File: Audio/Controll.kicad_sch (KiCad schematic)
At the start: 26 parts, among them J12 Conn_01x02_Pin, J13 Conn_01x02_Pin, J14 Conn_01x02_Pin, J15 Conn_01x02_Pin, J17 Conn_01x02_Pin, K1 AZ850P2-x, K10 AZ850P2-x, K2 AZ850P2-x, K3 AZ850P2-x, K4 AZ850P2-x, K5 AZ850P2-x, K6 AZ850P2-x, K7 AZ850P2-x, K8 AZ850P2-x, K9 AZ850P2-x, U4 BP5293-50, U5 ULN2803A, U6 ULN2803A, U7 ULN2803A

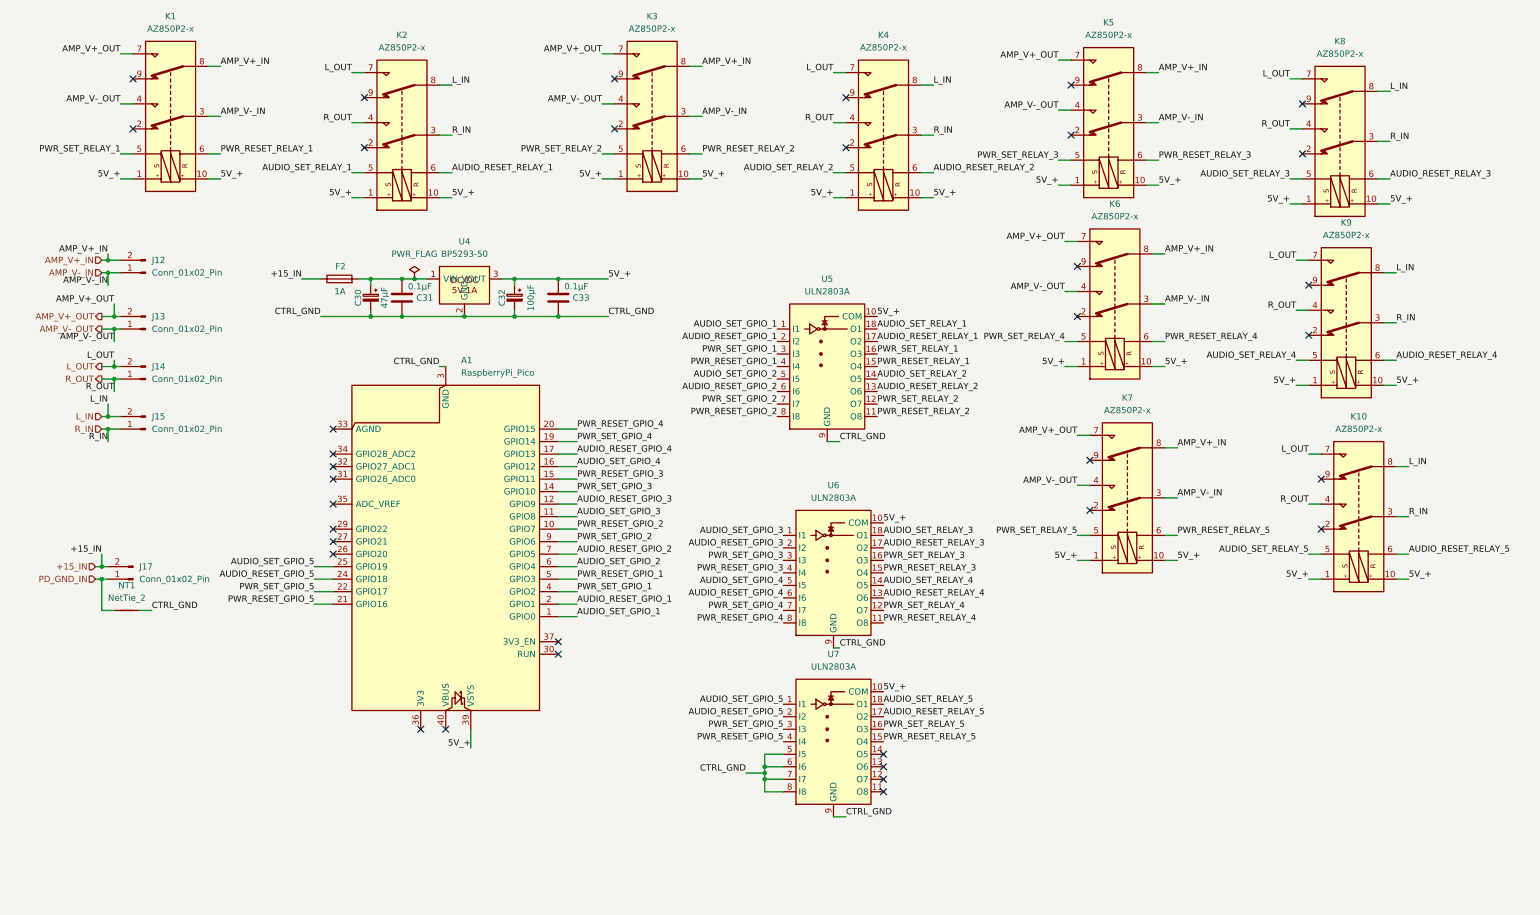
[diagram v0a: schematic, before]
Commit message: Audio: Controll端子・リレー配線とPCB部品配置まで反映。
ControllにAmp向け2P端子10個とリレー周りの回路を更新し、AudioCaseへフットプリントを配置。EQ/Amp/Controllは回路図レイアウトに合わせて部品位置を調整（PowerModuleは配線済みのため未変更）。BP5293-50フットプリント修正と配置用スクリプトを追加。

Co-authored-by: Cursor <cursoragent@cursor.com>
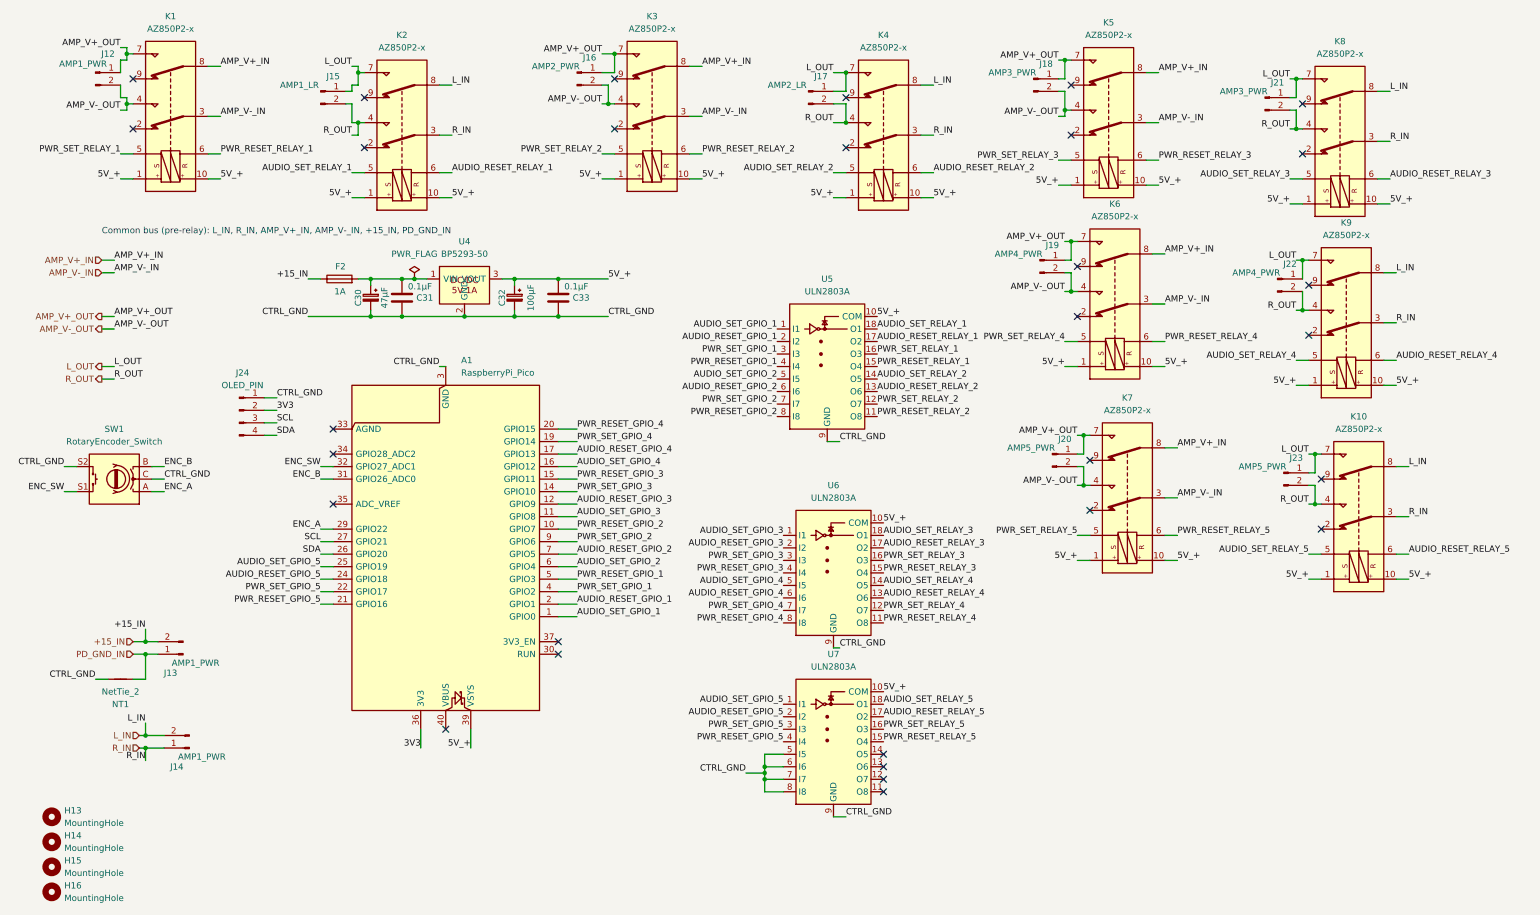
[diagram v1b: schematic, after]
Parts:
- added H13, H14, H15, H16: MountingHole, MountingHole:MountingHole_3.2mm_M3, symbol Mechanical:MountingHole
- added J16: AMP2_PWR, TerminalBlock_Phoenix:TerminalBlock_Phoenix_MKDS-1,5-2-5.08_1x02_P5.08mm_Horizontal, symbol Connector:Conn_01x02_Pin
- added J18, J21: AMP3_PWR, TerminalBlock_Phoenix:TerminalBlock_Phoenix_MKDS-1,5-2-5.08_1x02_P5.08mm_Horizontal, symbol Connector:Conn_01x02_Pin
- added J19, J22: AMP4_PWR, TerminalBlock_Phoenix:TerminalBlock_Phoenix_MKDS-1,5-2-5.08_1x02_P5.08mm_Horizontal, symbol Connector:Conn_01x02_Pin
- added J20, J23: AMP5_PWR, TerminalBlock_Phoenix:TerminalBlock_Phoenix_MKDS-1,5-2-5.08_1x02_P5.08mm_Horizontal, symbol Connector:Conn_01x02_Pin
- added J24: OLED_PIN, TerminalBlock_Phoenix:TerminalBlock_Phoenix_MKDS-1,5-4-5.08_1x04_P5.08mm_Horizontal, symbol Connector:Conn_01x04_Pin
- added SW1: RotaryEncoder_Switch, Rotary_Encoder:RotaryEncoder_Alps_EC11E-Switch_Vertical_H20mm, symbol Device:RotaryEncoder_Switch
- J12, J13, J14: value Conn_01x02_Pin -> AMP1_PWR; footprint (none) -> TerminalBlock_Phoenix:TerminalBlock_Phoenix_MKDS-1,5-2-5.08_1x02_P5.08mm_Horizontal
- J15: value Conn_01x02_Pin -> AMP1_LR; footprint (none) -> TerminalBlock_Phoenix:TerminalBlock_Phoenix_MKDS-1,5-2-5.08_1x02_P5.08mm_Horizontal
- J17: value Conn_01x02_Pin -> AMP2_LR; footprint (none) -> TerminalBlock_Phoenix:TerminalBlock_Phoenix_MKDS-1,5-2-5.08_1x02_P5.08mm_Horizontal
- NT1: footprint (none) -> NetTie:NetTie-2_THT_Pad1.0mm
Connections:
- net +15_IN: now also J13.2 (Pin_2); no longer J17.2 (Pin_2)
- net AMP_V+_IN: no longer J12.2 (Pin_2)
- net AMP_V+_OUT: now also J12.1 (Pin_1), J16.1 (Pin_1), J18.1 (Pin_1), J19.1 (Pin_1), J20.1 (Pin_1); no longer J13.2 (Pin_2)
- net AMP_V-_IN: no longer J12.1 (Pin_1)
- net AMP_V-_OUT: now also J12.2 (Pin_2), J16.2 (Pin_2), J18.2 (Pin_2), J19.2 (Pin_2), J20.2 (Pin_2); no longer J13.1 (Pin_1)
- net CTRL_GND: now also J24.1 (Pin_1), SW1.C, SW1.S2
- net L_IN: now also J14.2 (Pin_2); no longer J15.2 (Pin_2)
- net L_OUT: now also J15.1 (Pin_1), J17.1 (Pin_1), J21.1 (Pin_1), J22.1 (Pin_1), J23.1 (Pin_1); no longer J14.2 (Pin_2)
- net PD_GND_IN: now also J13.1 (Pin_1); no longer J17.1 (Pin_1)
- net R_IN: now also J14.1 (Pin_1); no longer J15.1 (Pin_1)
- net R_OUT: now also J15.2 (Pin_2), J17.2 (Pin_2), J21.2 (Pin_2), J22.2 (Pin_2), J23.2 (Pin_2); no longer J14.1 (Pin_1)
- net SDA: now reaches A1.26 (GPIO20)
- net SDA: now also J24.4 (Pin_4)
- net SCL: now reaches A1.27 (GPIO21)
- net SCL: now also J24.3 (Pin_3)
- net ENC_A: now reaches A1.29 (GPIO22)
- net ENC_A: now also SW1.A
- net ENC_B: now reaches A1.31 (GPIO26_ADC0)
- net ENC_B: now also SW1.B
- net ENC_SW: now reaches A1.32 (GPIO27_ADC1)
- net ENC_SW: now also SW1.S1
- net 3V3: now reaches A1.36 (3V3)
- net 3V3: now also J24.2 (Pin_2)
- no-connect marks 36 -> 30
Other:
- note added: "Common bus (pre-relay): L_IN, R_IN, AMP_V+_IN, AMP_V-_IN, +15_IN, PD_GND_IN"

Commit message: Update audio KiCad project wiring.
Co-authored-by: Cursor <cursoragent@cursor.com>
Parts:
- J13: value AMP1_PWR -> PD_IN
- J14: value AMP1_PWR -> AUDIO_IN
- J21: value AMP3_PWR -> AMP3_LR
- J22: value AMP4_PWR -> AMP4_LR
- J23: value AMP5_PWR -> AMP5_LR
- J24: footprint TerminalBlock_Phoenix:TerminalBlock_Phoenix_MKDS-1,5-4-5.08_1x04_P5.08mm_Horizontal -> Connector_PinHeader_1.00mm:PinHeader_1x04_P1.00mm_Vertical
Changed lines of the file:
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@@
 		(exclude_from_sim no)
 		(in_bom yes)
-		(on_board no)
+		(on_board yes)
 		(in_pos_files yes)
 		(dnp no)
@@
 			)
 		)
-		(property "Value" "AMP1_PWR"
+		(property "Value" "PD_IN"
 			(at 46.99 145.288 0)
 			(show_name no)
@@
 			)
 		)
-		(property "Footprint" "TerminalBlock_Phoenix:TerminalBlock_Phoenix_MKDS-1,5-4-5.08_1x04_P5.08mm_Horizontal"
+		(property "Footprint" "Connector_PinHeader_1.00mm:PinHeader_1x04_P1.00mm_Vertical"
 			(at 55.88 93.98 0)
 			(hide yes)
@@
 		(exclude_from_sim no)
 		(in_bom yes)
-		(on_board no)
+		(on_board yes)
 		(in_pos_files yes)
 		(dnp no)
@@
 		(exclude_from_sim no)
 		(in_bom yes)
-		(on_board no)
+		(on_board yes)
 		(in_pos_files yes)
 		(dnp no)
@@
 			)
 		)
-		(property "Value" "AMP1_PWR"
+		(property "Value" "AUDIO_IN"
 			(at 48.26 164.338 0)
 			(show_name no)
@@
 			)
 		)
-		(property "Value" "AMP4_PWR"
+		(property "Value" "AMP4_LR"
 			(at 262.382 66.04 0)
 			(show_name no)
@@
 			)
 		)
-		(property "Value" "AMP3_PWR"
+		(property "Value" "AMP3_LR"
 			(at 259.842 29.21 0)
 			(show_name no)
@@
 		(exclude_from_sim no)
 		(in_bom yes)
-		(on_board no)
+		(on_board yes)
 		(in_pos_files yes)
 		(dnp no)
@@
 		(exclude_from_sim no)
 		(in_bom yes)
-		(on_board no)
+		(on_board yes)
 		(in_pos_files yes)
 		(dnp no)
@@
 			)
 		)
-		(property "Value" "AMP5_PWR"
+		(property "Value" "AMP5_LR"
 			(at 263.652 105.41 0)
 			(show_name no)

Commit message: Controll基板のレイアウトを進め、AudioCase PCBと各シートを同期。
端子を上辺・入力左上・中央にリレー/ULN/Pico・下にUI・右に5Vとする配置へ更新。K1/K2のリレー接点配線とNetTieを含む回路図変更をPCBへ反映（PowerModuleの配線済み領域は維持）。

Co-authored-by: Cursor <cursoragent@cursor.com>
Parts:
- J13: renamed from SW1; value RotaryEncoder_Switch -> ROTARY_SW; footprint Rotary_Encoder:RotaryEncoder_Alps_EC11E-Switch_Vertical_H20mm -> Connector_PinHeader_2.54mm:PinHeader_1x05_P2.54mm_Vertical; symbol Device:RotaryEncoder_Switch -> Connector:Conn_01x05_Pin
- J16: renamed from J24; footprint Connector_PinHeader_1.00mm:PinHeader_1x04_P1.00mm_Vertical -> Connector_PinHeader_2.54mm:PinHeader_1x04_P2.54mm_Vertical
- renumbered J13 to J14, J14 to J15, J15 to J17, J16 to J18, J17 to J19, J18 to J20, J19 to J21, J20 to J22, J21 to J23, J22 to J24, J23 to J25
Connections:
- net 3V3: now also J13.4 (Pin_4)
- net AUDIO_RESET_GPIO_1: now also U5.7 (I7); no longer U5.2 (I2)
- net AUDIO_RESET_GPIO_2: now also U5.3 (I3); no longer U5.6 (I6)
- net AUDIO_RESET_GPIO_3: now also U6.7 (I7); no longer U6.2 (I2)
- net AUDIO_RESET_GPIO_4: now also U6.3 (I3); no longer U6.6 (I6)
- net AUDIO_RESET_GPIO_5: now also U7.3 (I3); no longer U7.2 (I2)
- net AUDIO_RESET_RELAY_1: now also U5.18 (O1); no longer U5.17 (O2)
- net AUDIO_RESET_RELAY_2: now also U5.14 (O5); no longer U5.13 (O6)
- net AUDIO_RESET_RELAY_3: now also U6.12 (O7); no longer U6.17 (O2)
- net AUDIO_RESET_RELAY_4: now also U6.16 (O3); no longer U6.13 (O6)
- net AUDIO_RESET_RELAY_5: now also U7.16 (O3); no longer U7.17 (O2)
- net AUDIO_SET_GPIO_1: now also U5.8 (I8); no longer U5.1 (I1)
- net AUDIO_SET_GPIO_2: now also U5.4 (I4); no longer U5.5 (I5)
- net AUDIO_SET_GPIO_3: now also U6.8 (I8); no longer U6.1 (I1)
- net AUDIO_SET_GPIO_4: now also U6.4 (I4); no longer U6.5 (I5)
- net AUDIO_SET_GPIO_5: now also U7.4 (I4); no longer U7.1 (I1)
- net AUDIO_SET_RELAY_1: now also U5.17 (O2); no longer U5.18 (O1)
- net AUDIO_SET_RELAY_2: now also U5.13 (O6); no longer U5.14 (O5)
- net AUDIO_SET_RELAY_3: now also U6.11 (O8); no longer U6.18 (O1)
- net AUDIO_SET_RELAY_4: now also U6.15 (O4); no longer U6.14 (O5)
- net AUDIO_SET_RELAY_5: now also U7.15 (O4); no longer U7.18 (O1)
- net CTRL_GND: now also J13.5 (Pin_5); no longer J13.C, J13.S2
- net ENC_A: now also J13.1 (Pin_1); no longer J13.A
- net ENC_B: now also J13.2 (Pin_2); no longer J13.B
- net ENC_SW: now also J13.3 (Pin_3); no longer J13.S1
- net PWR_RESET_GPIO_1: now also U5.5 (I5); no longer U5.4 (I4)
- net PWR_RESET_GPIO_2: now also U5.1 (I1); no longer U5.8 (I8)
- net PWR_RESET_GPIO_3: now also U6.5 (I5); no longer U6.4 (I4)
- net PWR_RESET_GPIO_4: now also U6.1 (I1); no longer U6.8 (I8)
- net PWR_RESET_GPIO_5: now also U7.1 (I1); no longer U7.4 (I4)
- net PWR_RESET_RELAY_1: now also U5.16 (O3); no longer U5.15 (O4)
- net PWR_RESET_RELAY_2: now also U5.12 (O7); no longer U5.11 (O8)
- net PWR_RESET_RELAY_3: now also U6.14 (O5); no longer U6.15 (O4)
- net PWR_RESET_RELAY_4: now also U6.18 (O1); no longer U6.11 (O8)
- net PWR_RESET_RELAY_5: now also U7.18 (O1); no longer U7.15 (O4)
- net PWR_SET_GPIO_1: now also U5.6 (I6); no longer U5.3 (I3)
- net PWR_SET_GPIO_2: now also U5.2 (I2); no longer U5.7 (I7)
- net PWR_SET_GPIO_3: now also U6.6 (I6); no longer U6.3 (I3)
- net PWR_SET_GPIO_4: now also U6.2 (I2); no longer U6.7 (I7)
- net PWR_SET_GPIO_5: now also U7.2 (I2); no longer U7.3 (I3)
- net PWR_SET_RELAY_1: now also U5.15 (O4); no longer U5.16 (O3)
- net PWR_SET_RELAY_2: now also U5.11 (O8); no longer U5.12 (O7)
- net PWR_SET_RELAY_3: now also U6.13 (O6); no longer U6.16 (O3)
- net PWR_SET_RELAY_4: now also U6.17 (O2); no longer U6.12 (O7)
- net PWR_SET_RELAY_5: now also U7.17 (O2); no longer U7.16 (O3)

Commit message: AudioCaseを製造用に4基板へ分割
KiKitで切り出した個別PCBとGerber/ドリル出力を追加し、JLCPCB向けに各基板を個別発注できる形にします。

Co-authored-by: Cursor <cursoragent@cursor.com>
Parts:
- added J14: AMP_PWR_IN, TerminalBlock_Phoenix:TerminalBlock_Phoenix_MKDS-1,5-2-5.08_1x02_P5.08mm_Horizontal, symbol Connector:Conn_01x02_Pin
- renumbered J14 to J15, J15 to J16, J16 to J17, J17 to J18, J18 to J19, J19 to J20, J20 to J21, J21 to J22, J22 to J23, J23 to J24, J24 to J25, J25 to J26
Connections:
- net AMP_V+_IN: now also J14.1 (Pin_1)
- net AMP_V-_IN: now also J14.2 (Pin_2)
- net AUDIO_RESET_GPIO_5: now also U7.1 (I1); no longer U7.3 (I3)
- net AUDIO_RESET_RELAY_5: now also U7.18 (O1); no longer U7.16 (O3)
- net AUDIO_SET_GPIO_5: now also U7.2 (I2); no longer U7.4 (I4)
- net AUDIO_SET_RELAY_5: now also U7.17 (O2); no longer U7.15 (O4)
- net PWR_RESET_GPIO_5: now also U7.3 (I3); no longer U7.1 (I1)
- net PWR_RESET_RELAY_5: now also U7.16 (O3); no longer U7.18 (O1)
- net PWR_SET_GPIO_5: now also U7.4 (I4); no longer U7.2 (I2)
- net PWR_SET_RELAY_5: now also U7.15 (O4); no longer U7.17 (O2)

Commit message: ノイズ対策と製造データ整備: デカップリング追加・GNDベタ強化・シルク整理
- 5V_+ラインにデカップリング/バルク(C34-C37)を追加し、リレー切替時の電源変動を抑制
- F.CuにCTRL_GND/GNDベタを追加し、ステッチングビアで表裏GNDを補強(DC-DC周辺含む)
- 端子台ラベル等のシルク重なりを解消(J11/J14/J6/J4/L1/L2ほか)
- masterから4基板を再split、Gerber/zipを再生成

Co-authored-by: Cursor <cursoragent@cursor.com>
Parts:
- added C34, C35, C36, C37: 0.1μF, Capacitor_SMD:C_1206_3216Metric_Pad1.33x1.80mm_HandSolder, symbol Device:C
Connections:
- net 5V_+: now also C34.2, C35.2, C36.2, C37.2
- net CTRL_GND: now also C34.1, C35.1, C36.1, C37.1
